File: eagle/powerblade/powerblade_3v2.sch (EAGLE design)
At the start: 78 parts, among them J1 JTAG_14PIN_IDC-ND, J2 AC_INF3, J4 TC2030-JLINK-NL, Q1 NTS4173, Q4 2SK1829, U1 TPS62122, U2 MCP6V3, U3 MSP430FR5738, U4 NRF51822QF, U6 MAX9910, U7 OPA2369, X1 16MHz, X3 32.768kHz, Y1 UREACH_XTEND

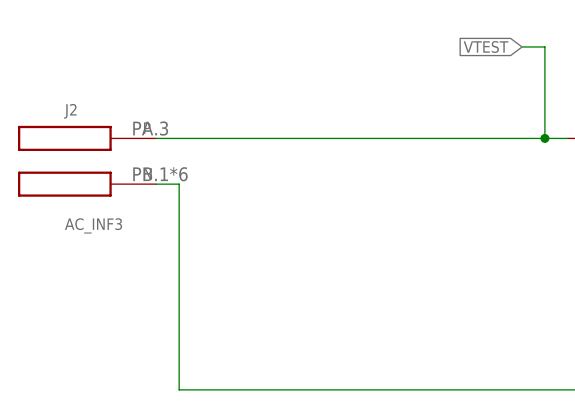
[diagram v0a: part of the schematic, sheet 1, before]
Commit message: added PA.1 to phase connection in AC_F3
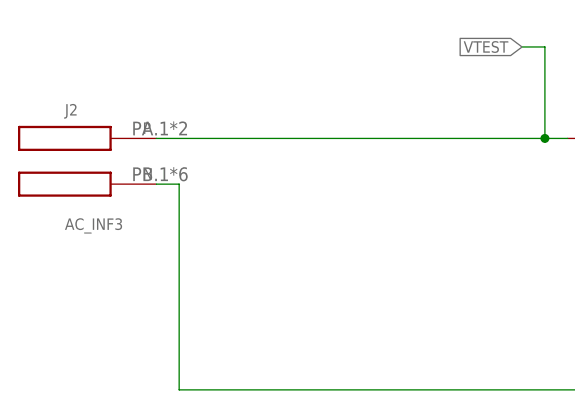
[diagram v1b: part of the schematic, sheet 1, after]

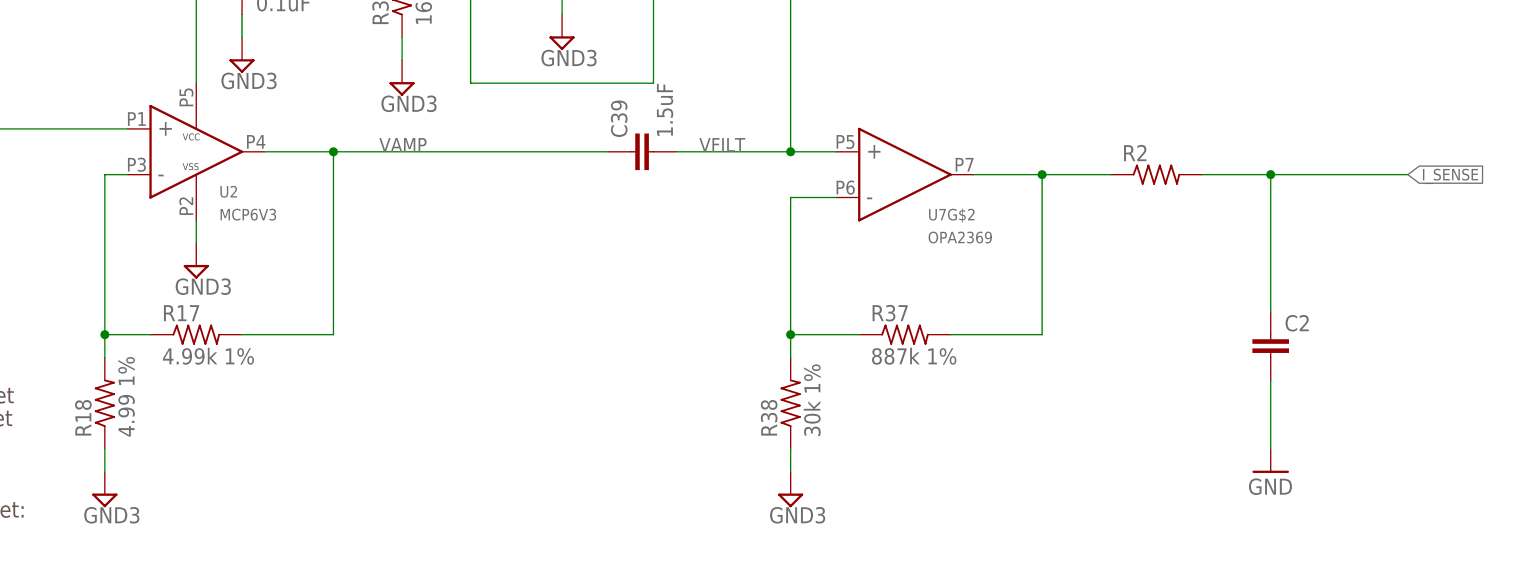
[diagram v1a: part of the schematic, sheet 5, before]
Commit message: all parts in pb3v2 have part numbers
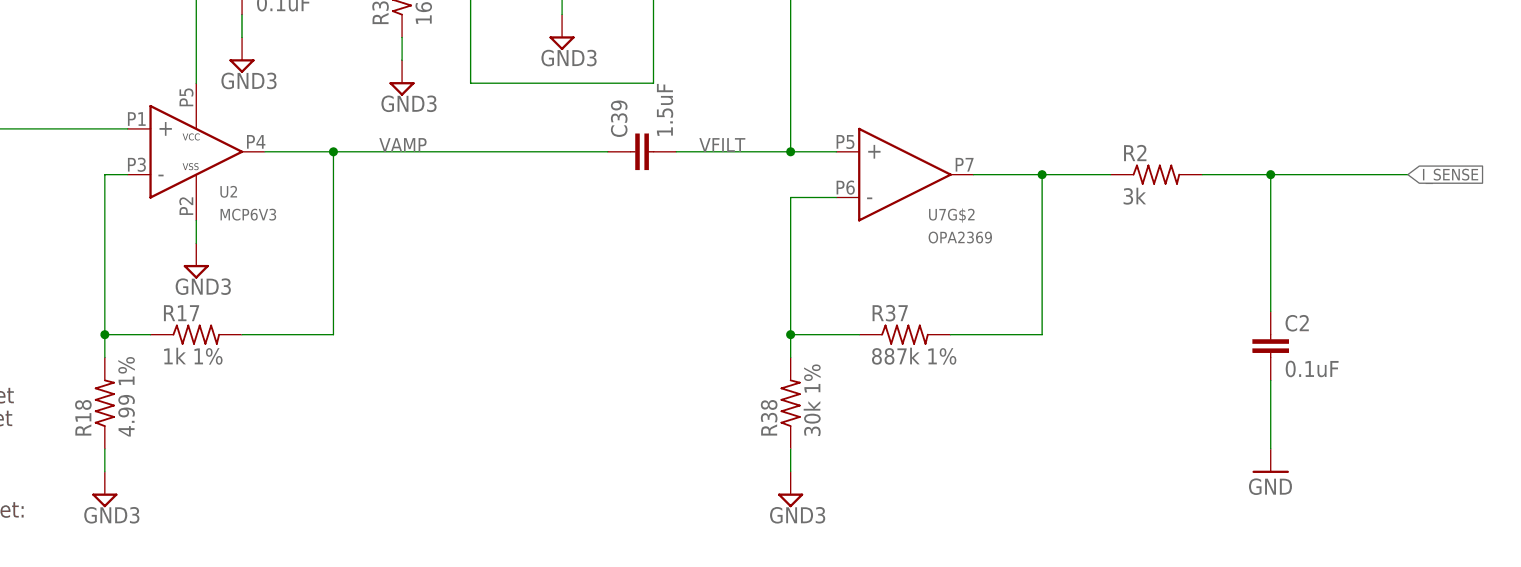
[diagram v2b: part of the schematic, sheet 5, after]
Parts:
- C1: DIGIKEY_2 478-8654-1-ND -> (none)
- C2: value (none) -> 0.1uF; DIGIKEY (none) -> 490-10777-1-ND
- R17: value 4.99k 1% -> 1k 1%; DIGIKEY P4.99KLCT-ND -> P1.00KLCT-ND; DIGIKEY_2 P10.0KLCT-ND -> (none)
- R18: DIGIKEY_2 P10.0LCT-ND -> (none)
- R2: value (none) -> 3k; DIGIKEY (none) -> P3.00KLCT-ND
- R3: value 80k -> 69.8k; DIGIKEY P80.6KAACT-ND -> P69.8KAACT-ND; DIGIKEY_2 P69.8KAACT-ND -> (none); DIGIKEY_3 P40.2KAACT-ND -> (none)
- R35: DIGIKEY P2.00KLCT-ND -> P20.0KLCT-ND; DIGIKEY_2 P20.0KLCT-ND -> (none)
- U2: DIGIKEY (none) -> 296-19547-1-ND; DIGIKEY_POP 296-19547-1-ND -> (none)
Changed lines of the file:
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@@
 <attribute name="DIGIKEY" value="P75.0LCT-ND"/>
 </part>
-<part name="R17" library="rcl" deviceset="R-US_" device="R0402" value="4.99k 1%">
-<attribute name="DIGIKEY" value="P4.99KLCT-ND"/>
-<attribute name="DIGIKEY_2" value="P10.0KLCT-ND"/>
+<part name="R17" library="rcl" deviceset="R-US_" device="R0402" value="1k 1%">
+<attribute name="DIGIKEY" value="P1.00KLCT-ND"/>
 </part>
 <part name="R18" library="rcl" deviceset="R-US_" device="R0402" value="4.99 1%">
 <attribute name="DIGIKEY" value="RMCF0402FT4R99CT-ND"/>
-<attribute name="DIGIKEY_2" value="P10.0LCT-ND"/>
 </part>
 <part name="C27" library="rcl" deviceset="C-EU" device="C0402" value="0.1uF">
@@
 <part name="+3V3" library="supply1" deviceset="+3V3" device=""/>
 <part name="R35" library="rcl" deviceset="R-US_" device="R0402" value="20k">
-<attribute name="DIGIKEY" value="P2.00KLCT-ND"/>
-<attribute name="DIGIKEY_2" value="P20.0KLCT-ND"/>
+<attribute name="DIGIKEY" value="P20.0KLCT-ND"/>
 </part>
 <part name="R37" library="rcl" deviceset="R-US_" device="R0402" value="887k 1%">
@@
 <attribute name="DIGIKEY" value="P16.0KLCT-ND"/>
 </part>
-<part name="R2" library="rcl" deviceset="R-US_" device="R0402_SM"/>
-<part name="C2" library="rcl" deviceset="C-EU" device="C0402"/>
+<part name="R2" library="rcl" deviceset="R-US_" device="R0402_SM" value="3k">
+<attribute name="DIGIKEY" value="P3.00KLCT-ND"/>
+</part>
+<part name="C2" library="rcl" deviceset="C-EU" device="C0402" value="0.1uF">
+<attribute name="DIGIKEY" value="490-10777-1-ND"/>
+</part>
 <part name="U2" library="powerfilm" deviceset="MCP6V3" device="">
-<attribute name="DIGIKEY_POP" value="296-19547-1-ND"/>
-</part>
-<part name="R3" library="rcl" deviceset="R-US_" device="R1210" value="80k">
-<attribute name="DIGIKEY" value="P80.6KAACT-ND"/>
-<attribute name="DIGIKEY_2" value="P69.8KAACT-ND"/>
-<attribute name="DIGIKEY_3" value="P40.2KAACT-ND"/>
+<attribute name="DIGIKEY" value="296-19547-1-ND"/>
+</part>
+<part name="R3" library="rcl" deviceset="R-US_" device="R1210" value="69.8k">
+<attribute name="DIGIKEY" value="P69.8KAACT-ND"/>
 </part>
 <part name="U3" library="powerfilm" deviceset="MSP430FR5738" device=""/>
@@
 <part name="C1" library="rcl" deviceset="CPOL-US" device="0805_SM" value="33uF">
 <attribute name="DIGIKEY" value="478-8650-1-ND"/>
-<attribute name="DIGIKEY_2" value="478-8654-1-ND"/>
 </part>
 <part name="C5" library="rcl" deviceset="C-EU" device="C0603_TN" value="NP">
@@
 <instance part="R3" gate="G$1" x="15.24" y="17.78">
 <attribute name="DIGIKEY" x="15.24" y="17.78" size="1.27" layer="96" display="off"/>
-<attribute name="DIGIKEY_2" x="15.24" y="17.78" size="1.27" layer="96" display="off"/>
-<attribute name="DIGIKEY_3" x="15.24" y="17.78" size="1.27" layer="96" display="off"/>
 </instance>
 <instance part="C1" gate="G$1" x="104.14" y="5.08">
 <attribute name="DIGIKEY" x="104.14" y="5.08" size="1.27" layer="96" display="off"/>
-<attribute name="DIGIKEY_2" x="104.14" y="5.08" size="1.27" layer="96" display="off"/>
 </instance>
 <instance part="J2" gate="G$1" x="-43.18" y="15.24">
@@
 <instance part="R17" gate="G$1" x="93.98" y="-30.48">
 <attribute name="DIGIKEY" x="93.98" y="-30.48" size="1.27" layer="96" display="off"/>
-<attribute name="DIGIKEY_2" x="93.98" y="-30.48" size="1.27" layer="96" display="off"/>
 </instance>
 <instance part="R18" gate="G$1" x="83.82" y="-38.1" rot="R90">
 <attribute name="DIGIKEY" x="83.82" y="-38.1" size="1.27" layer="96" rot="R90" display="off"/>
-<attribute name="DIGIKEY_2" x="83.82" y="-38.1" size="1.27" layer="96" rot="R90" display="off"/>
 </instance>
 <instance part="C27" gate="G$1" x="99.06" y="10.16">
@@
 <instance part="R35" gate="G$1" x="152.4" y="15.24">
 <attribute name="DIGIKEY" x="152.4" y="15.24" size="1.27" layer="96" display="off"/>
-<attribute name="DIGIKEY_2" x="152.4" y="15.24" size="1.27" layer="96" display="off"/>
 </instance>
 <instance part="R37" gate="G$1" x="172.72" y="-30.48">
@@
 <attribute name="DIGIKEY" x="116.84" y="7.62" size="1.27" layer="96" rot="R90" display="off"/>
 </instance>
-<instance part="R2" gate="G$1" x="200.66" y="-12.7"/>
-<instance part="C2" gate="G$1" x="213.36" y="-30.48"/>
-<instance part="U2" gate="G$1" x="93.98" y="-10.16">
-<attribute name="DIGIKEY_POP" x="93.98" y="-10.16" size="1.27" layer="96" display="off"/>
-</instance>
+<instance part="R2" gate="G$1" x="200.66" y="-12.7">
+<attribute name="DIGIKEY" x="200.66" y="-12.7" size="1.27" layer="96" display="off"/>
+</instance>
+<instance part="C2" gate="G$1" x="213.36" y="-30.48">
+<attribute name="DIGIKEY" x="213.36" y="-30.48" size="1.27" layer="96" display="off"/>
+</instance>
+<instance part="U2" gate="G$1" x="93.98" y="-10.16"/>
 <instance part="SUPPLY15" gate="G$1" x="-20.32" y="-5.08"/>
 <instance part="SUPPLY16" gate="G$1" x="-27.94" y="-25.4"/>

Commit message: added pogo part number
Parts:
- J2: DIGIKEY NP -> ED1649-ND; DIGIKEY_2 (none) -> ED1649-ND; DIGIKEY_3 (none) -> ED1649-ND; DIGIKEY_4 (none) -> ED1649-ND
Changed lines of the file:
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@@
 </part>
 <part name="J2" library="powerfilm" deviceset="AC_IN" device="F3" value="AC_INF3">
-<attribute name="DIGIKEY" value="NP"/>
+<attribute name="DIGIKEY" value="ED1649-ND"/>
+<attribute name="DIGIKEY_2" value="ED1649-ND"/>
+<attribute name="DIGIKEY_3" value="ED1649-ND"/>
+<attribute name="DIGIKEY_4" value="ED1649-ND"/>
 </part>
 <part name="Q1" library="powerfilm" deviceset="NTS4173" device=""/>
@@
 <instance part="J2" gate="G$1" x="-43.18" y="15.24">
 <attribute name="DIGIKEY" x="-43.18" y="15.24" size="1.27" layer="96" display="off"/>
+<attribute name="DIGIKEY_2" x="-43.18" y="15.24" size="1.27" layer="96" display="off"/>
+<attribute name="DIGIKEY_3" x="-43.18" y="15.24" size="1.27" layer="96" display="off"/>
+<attribute name="DIGIKEY_4" x="-43.18" y="15.24" size="1.27" layer="96" display="off"/>
 </instance>
 </instances>
